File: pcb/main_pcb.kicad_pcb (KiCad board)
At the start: 2 copper layers, 62 x 67 mm, 44 parts, among them J1 Conn_01x06_Socket, J2 Conn_01x10_Pin, J4 USB_C_Receptacle_USB2.0, Q1 Si2323DS, SW1 SW_Push, SW2 SW_Push, SW3 SW_Push, U1 ESP32-H2-MINI-1, U2 LM5165Y, Y1 32.768KHz

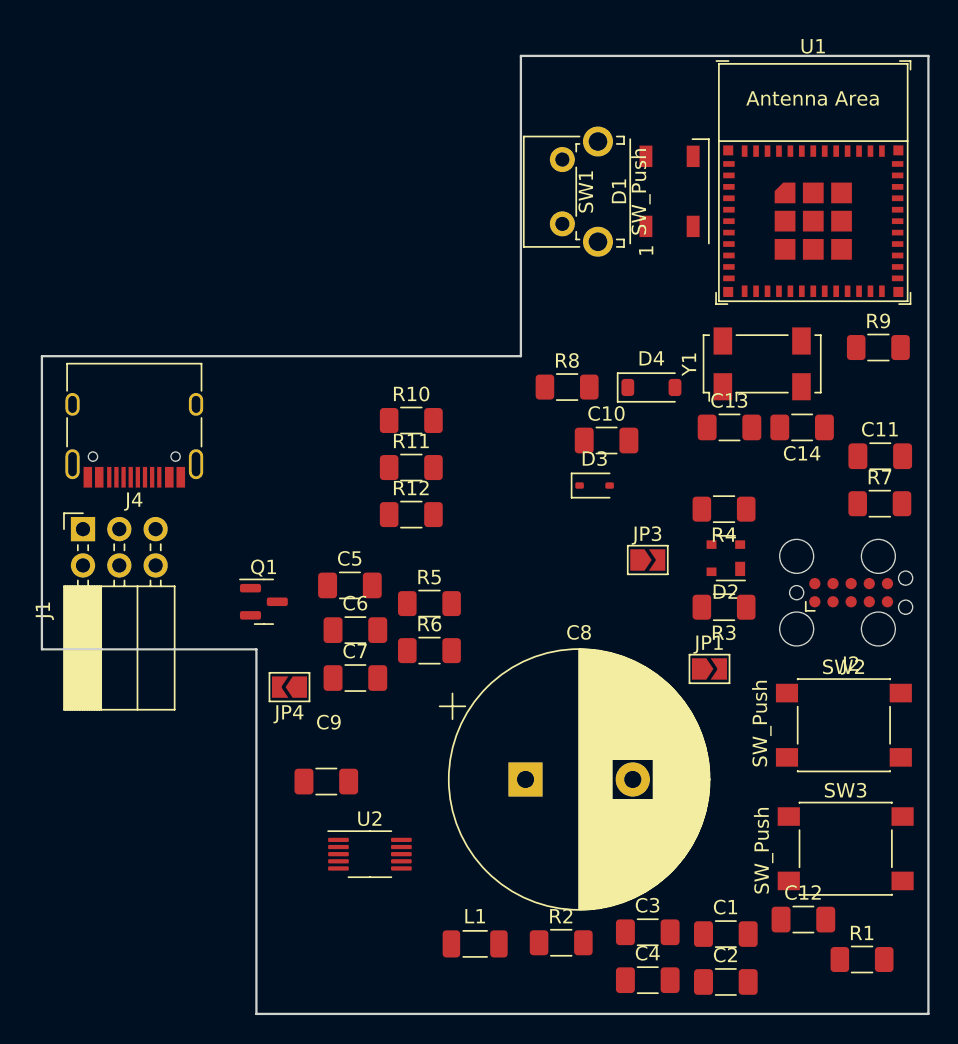
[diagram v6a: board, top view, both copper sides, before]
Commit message: Add keep out areas to PCB
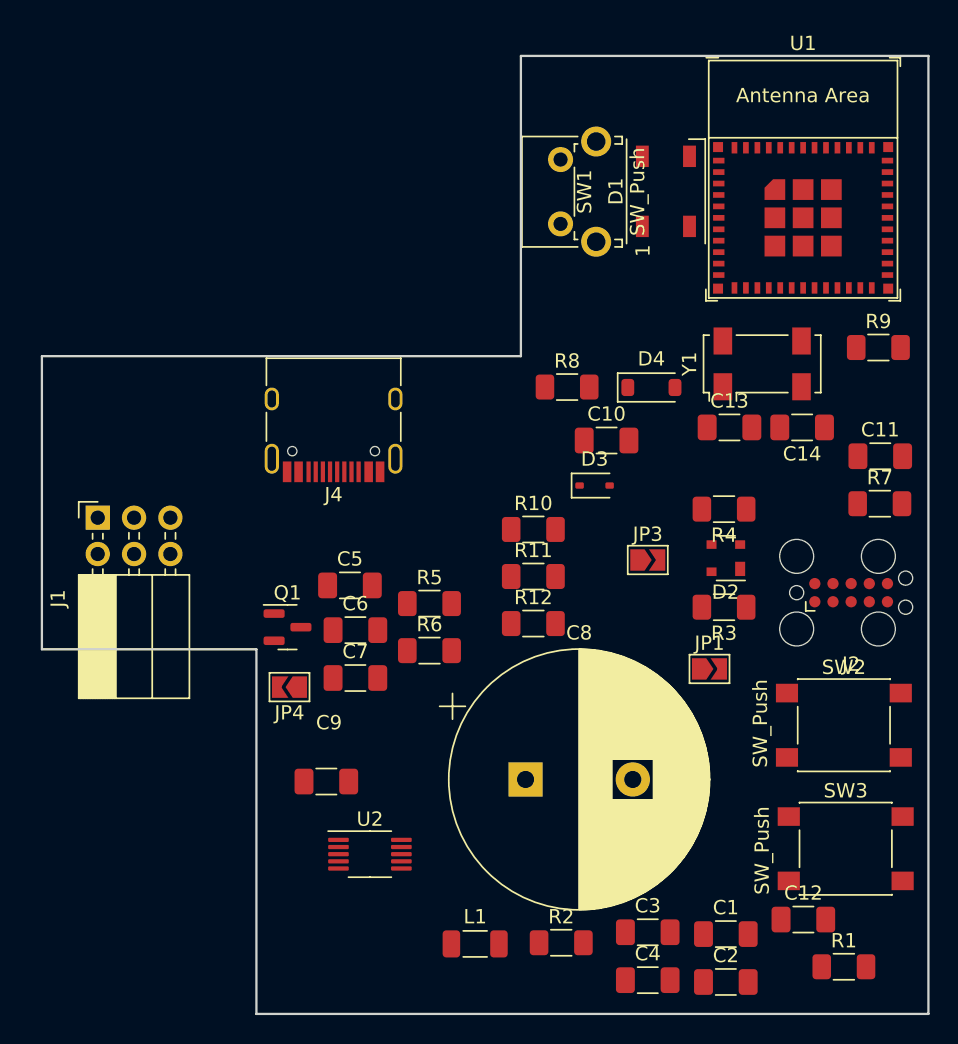
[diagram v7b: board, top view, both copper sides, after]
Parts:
- moved J4 13.9 mm to (129.4, 68.3)
- moved R10 11.4 mm to (143.4, 76.4)
- moved R11 11.4 mm to (143.4, 79.6)
- moved R12 11.4 mm to (143.4, 82.9)
- moved Q1 2.43 mm to (126.2, 83.2)
- moved R1 1.37 mm to (165.1, 106.9)
- moved J1 1.30 mm to (112.9, 75.5)
- moved U1 0.75 mm to (162.2, 51.9)
- moved D1 0.25 mm to (152.7, 52.7)
- moved SW1 0.13 mm to (145.3, 55.0)
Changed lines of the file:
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@@
   )
   (footprint "Button_Switch_THT:SW_Tactile_SPST_Angled_PTS645Vx31-2LFS" (layer "F.Cu")
-    (at 145.4125 54.98 90)
+    (at 145.2855 54.98 90)
     (descr "tactile switch SPST right angle, PTS645VL31-2 LFS")
     (tags "tactile switch SPST angled PTS645VL31-2 LFS C&K Button")
@@
   )
   (footprint "Package_TO_SOT_SMD:SOT-23" (layer "F.Cu")
-    (at 124.5385 81.407)
+    (at 126.1895 83.185)
     (descr "SOT, 3 Pin (https://www.jedec.org/system/files/docs/to-236h.pdf variant AB), generated with kicad-footprint-generator ipc_gullwing_generator.py")
     (tags "SOT TO_SOT_SMD")
@@
   )
   (footprint "Connector_USB:USB_C_Receptacle_HRO_TYPE-C-31-M-12" (layer "F.Cu")
-    (at 115.474 68.655 180)
+    (at 129.413 68.274 180)
     (descr "USB Type-C receptacle for USB 2.0 and PD, http://www.krhro.com/uploads/soft/180320/1-1P320120243.pdf")
     (tags "usb usb-c 2.0 pd")
@@
   )
   (footprint "Resistor_SMD:R_1206_3216Metric_Pad1.30x1.75mm_HandSolder" (layer "F.Cu")
-    (at 134.848 68.731)
+    (at 143.383 76.351)
     (descr "Resistor SMD 1206 (3216 Metric), square (rectangular) end terminal, IPC_7351 nominal with elongated pad for handsoldering. (Body size source: IPC-SM-782 page 72, https://www.pcb-3d.com/wordpress/wp-content/uploads/ipc-sm-782a_amendment_1_and_2.pdf), generated with kicad-footprint-generator")
     (tags "resistor handsolder")
@@
   )
   (footprint "PCM_Espressif:ESP32-H2-MINI-1" (layer "F.Cu")
-    (at 162.96 52.09)
+    (at 162.249 51.857)
     (descr "ESP32-H2-MINI-1: https://www.espressif.com/sites/default/files/documentation/esp32-h2-mini-1_mini-1u_datasheet_en.pdf")
     (tags "ESP32-H2")
@@
       (polygon
         (pts
-          (xy 169.56 49.19)
-          (xy 156.36 49.19)
-          (xy 156.36 43.79)
-          (xy 169.56 43.79)
+          (xy 168.849 48.957)
+          (xy 155.649 48.957)
+          (xy 155.649 43.557)
+          (xy 168.849 43.557)
         )
       )
@@
   )
   (footprint "Resistor_SMD:R_1206_3216Metric_Pad1.30x1.75mm_HandSolder" (layer "F.Cu")
-    (at 134.848 72.021)
+    (at 143.383 79.641)
     (descr "Resistor SMD 1206 (3216 Metric), square (rectangular) end terminal, IPC_7351 nominal with elongated pad for handsoldering. (Body size source: IPC-SM-782 page 72, https://www.pcb-3d.com/wordpress/wp-content/uploads/ipc-sm-782a_amendment_1_and_2.pdf), generated with kicad-footprint-generator")
     (tags "resistor handsolder")
@@
   )
   (footprint "Resistor_SMD:R_1206_3216Metric_Pad1.30x1.75mm_HandSolder" (layer "F.Cu")
-    (at 166.37 106.426)
+    (at 165.1 106.934)
     (descr "Resistor SMD 1206 (3216 Metric), square (rectangular) end terminal, IPC_7351 nominal with elongated pad for handsoldering. (Body size source: IPC-SM-782 page 72, https://www.pcb-3d.com/wordpress/wp-content/uploads/ipc-sm-782a_amendment_1_and_2.pdf), generated with kicad-footprint-generator")
     (tags "resistor handsolder")
@@
   )
   (footprint "LED_SMD:LED_WS2812B_PLCC4_5.0x5.0mm_P3.2mm" (layer "F.Cu")
-    (at 152.908 52.705 90)
+    (at 152.654 52.705 90)
     (descr "5.0mm x 5.0mm Addressable RGB LED NeoPixel, https://cdn-shop.adafruit.com/datasheets/WS2812B.pdf")
     (tags "LED RGB NeoPixel PLCC-4 5050")
@@
   )
   (footprint "Connector_PinSocket_2.54mm:PinSocket_2x03_P2.54mm_Horizontal" (layer "F.Cu")
-    (at 111.887 76.327 90)
+    (at 112.918 75.528 90)
     (descr "Through hole angled socket strip, 2x03, 2.54mm pitch, 8.51mm socket length, double cols (from Kicad 4.0.7), script generated")
     (tags "Through hole angled socket strip THT 2x03 2.54mm double row")
@@
   )
   (footprint "Resistor_SMD:R_1206_3216Metric_Pad1.30x1.75mm_HandSolder" (layer "F.Cu")
-    (at 134.848 75.311)
+    (at 143.383 82.931)
     (descr "Resistor SMD 1206 (3216 Metric), square (rectangular) end terminal, IPC_7351 nominal with elongated pad for handsoldering. (Body size source: IPC-SM-782 page 72, https://www.pcb-3d.com/wordpress/wp-content/uploads/ipc-sm-782a_amendment_1_and_2.pdf), generated with kicad-footprint-generator")
     (tags "resistor handsolder")
@@
   (gr_line (start 109.012375 64.232094) (end 109.012375 84.732094)
     (stroke (width 0.16) (type solid)) (layer "Edge.Cuts"))
+  (zone locked (net 0) (net_name "") (layers "F&B.Cu" "*.SilkS") (name "corner") (hatch edge 0.5)
+    (connect_pads (clearance 0))
+    (min_thickness 0.25) (filled_areas_thickness no)
+    (keepout (tracks allowed) (vias allowed) (pads not_allowed) (copperpour allowed) (footprints not_allowed))
+    (fill (thermal_gap 0.5) (thermal_bridge_width 0.5))
+    (polygon
+      (pts
+        (xy 171.069 110.236)
+        (xy 171.069 108.331026)
+        (xy 169.095105 108.32633)
+        (xy 169.095105 110.236026)
+      )
+    )
+  )
+  (zone locked (net 0) (net_name "") (layers "F&B.Cu" "*.SilkS") (name "corner") (hatch edge 0.5)
+    (connect_pads (clearance 0))
+    (min_thickness 0.25) (filled_areas_thickness no)
+    (keepout (tracks allowed) (vias allowed) (pads not_allowed) (copperpour allowed) (footprints not_allowed))
+    (fill (thermal_gap 0.5) (thermal_bridge_width 0.5))
+    (polygon
+      (pts
+        (xy 125.984 110.236)
+        (xy 125.984 108.331026)
+        (xy 124.010105 108.32633)
+        (xy 124.010105 110.236026)
+      )
+    )
+  )
+  (zone locked (net 0) (net_name "") (layers "F&B.Cu" "*.SilkS") (name "corner") (hatch edge 0.5)
+    (connect_pads (clearance 0))
+    (min_thickness 0.25) (filled_areas_thickness no)
+    (keepout (tracks allowed) (vias allowed) (pads not_allowed) (copperpour allowed) (footprints not_allowed))
+    (fill (thermal_gap 0.5) (thermal_bridge_width 0.5))
+    (polygon
+      (pts
+        (xy 110.997994 84.712298)
+        (xy 110.997994 64.265324)
+        (xy 109.024099 64.260628)
+        (xy 109.024099 84.712324)
+      )
+    )
+  )
+  (zone locked (net 0) (net_name "") (layers "F&B.Cu" "*.SilkS") (name "corner") (hatch edge 0.5)
+    (connect_pads (clearance 0))
+    (min_thickness 0.25) (filled_areas_thickness no)
+    (keepout (tracks allowed) (vias allowed) (pads not_allowed) (copperpour allowed) (footprints not_allowed))
+    (fill (thermal_gap 0.5) (thermal_bridge_width 0.5))
+    (polygon
+      (pts
+        (xy 171.068995 45.087089)
+        (xy 171.068995 43.182115)
+        (xy 169.0951 43.177419)
+        (xy 169.0951 45.087115)
+      )
+    )
+  )
+  (zone locked (net 0) (net_name "") (layers "B.Cu" "B.SilkS") (name "flap") (hatch edge 0.5)
+    (connect_pads (clearance 0))
+    (min_thickness 0.25) (filled_areas_thickness no)
+    (keepout (tracks allowed) (vias allowed) (pads not_allowed) (copperpour allowed) (footprints not_allowed))
+    (fill (thermal_gap 0.5) (thermal_bridge_width 0.5))
+    (polygon
+      (pts
+        (xy 124.003025 84.704304)
+        (xy 124.079 64.262)
+        (xy 120.066025 64.257304)
+        (xy 120.066025 84.709)
+      )
+    )
+  )
 )

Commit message: Remove JTAG connector
Planning on using the built in JTAG via USB.
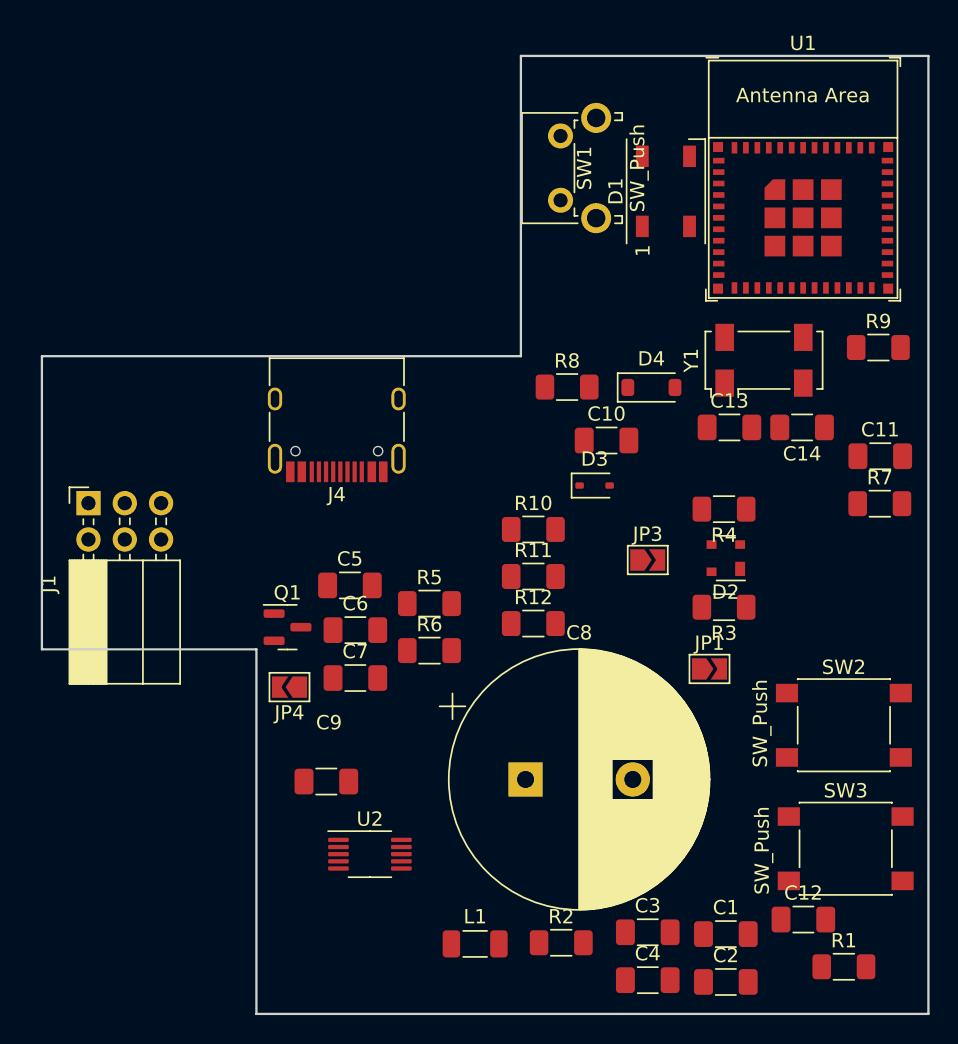
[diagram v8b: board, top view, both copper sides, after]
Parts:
- removed J2: Conn_01x10_Pin, Connector:Tag-Connect_TC2050-IDC-FP_2x05_P1.27mm_Vertical
- moved SW1 1.65 mm to (145.3, 53.3)
- moved J1 1.21 mm to (112.3, 74.5)
- moved Y1 0.28 mm to (159.5, 64.5)
- moved J4 0.22 mm to (129.6, 68.3)
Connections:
- U1 pad 18: /TCK -> unconnected-(U1-GPIO4/FSPICLK/ADC1_CH3/MTCK-Pad18)
- U1 pad 19: /TDI -> unconnected-(U1-GPIO5/FSPID/ADC1_CH4/MTDI-Pad19)
- U1 pad 5: /TMS -> unconnected-(U1-GPIO2/FSPIWP/ADC1_CH1/MTMS-Pad5)
- U1 pad 6: /TDO -> unconnected-(U1-GPIO3/FSPIHD/ADC1_CH2/MTDO-Pad6)
